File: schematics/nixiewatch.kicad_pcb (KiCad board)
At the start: 2 copper layers, 70 x 50 mm, 21 parts, among them Q1 BC546, Q2 6N90C, U1 NE555P

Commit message: pcb layout
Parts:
- removed +BATT: +8V, Connector_Pin:Pin_D0.7mm_L6.5mm_W1.8mm_FlatFork
- removed REF**: GND, Connector_Pin:Pin_D0.7mm_L6.5mm_W1.8mm_FlatFork
- removed REF**: +170V, Connector_Pin:Pin_D0.7mm_L6.5mm_W1.8mm_FlatFork
- added C5: 33u, Capacitor_THT:CP_Radial_D4.0mm_P1.50mm, F.Cu at (83.6, 129.8)
- added N1: IN-16, Connector_PinHeader_2.00mm:PinHeader_1x13_P2.00mm_Vertical, F.Cu at (48.9, 169.8)
- added N2: IN-16, Connector_PinHeader_2.00mm:PinHeader_1x13_P2.00mm_Vertical, F.Cu at (101.4, 169.8)
- added Q3: BC546, Package_TO_SOT_THT:TO-92_Inline, F.Cu at (63.0, 148.6)
- added R10: 20k, Resistor_THT:R_Axial_DIN0207_L6.3mm_D2.5mm_P7.62mm_Horizontal, F.Cu at (71.2, 123.2)
- added R11: 20k, Resistor_THT:R_Axial_DIN0207_L6.3mm_D2.5mm_P7.62mm_Horizontal, F.Cu at (64.3, 129.6)
- added R12: 47k, Resistor_THT:R_Axial_DIN0207_L6.3mm_D2.5mm_P7.62mm_Horizontal, F.Cu at (87.5, 151.6)
- added R13: 6k8, Resistor_THT:R_Axial_DIN0207_L6.3mm_D2.5mm_P7.62mm_Horizontal, F.Cu at (61.0, 146.0)
- added R14: 2k2, Resistor_THT:R_Axial_DIN0207_L6.3mm_D2.5mm_P7.62mm_Horizontal, F.Cu at (81.4, 151.6)
- added R15: 20k, Resistor_THT:R_Axial_DIN0207_L6.3mm_D2.5mm_P7.62mm_Horizontal, F.Cu at (67.5, 151.7)
- added R16: 100k, Resistor_THT:R_Axial_DIN0207_L6.3mm_D2.5mm_P7.62mm_Horizontal, F.Cu at (68.4, 166.8)
- added R17: 100k, Resistor_THT:R_Axial_DIN0207_L6.3mm_D2.5mm_P7.62mm_Horizontal, F.Cu at (86.7, 166.8)
- added R18: 100k, Resistor_THT:R_Axial_DIN0207_L6.3mm_D2.5mm_P7.62mm_Horizontal, F.Cu at (101.4, 161.2)
- added R19: 100k, Resistor_THT:R_Axial_DIN0207_L6.3mm_D2.5mm_P7.62mm_Horizontal, F.Cu at (101.4, 143.8)
- added R9: 20k, Resistor_THT:R_Axial_DIN0207_L6.3mm_D2.5mm_P7.62mm_Horizontal, F.Cu at (71.2, 119.8)
- added U2: TPIC6B595, Package_DIP:DIP-20_W7.62mm, F.Cu at (50.4, 142.8)
- added U3: 5V MCP1702, Package_TO_SOT_THT:TO-92_Inline, F.Cu at (83.6, 135.7)
- added U4: TPIC6B595, Package_DIP:DIP-20_W7.62mm, F.Cu at (63.4, 164.2)
- added U5: TPIC6B595, Package_DIP:DIP-20_W7.62mm, F.Cu at (91.0, 143.2)
- added U6: ATtiny45V-10P, Package_DIP:DIP-8_W7.62mm, F.Cu at (64.4, 132.7)
- added U7: DS1307+, Package_DIP:DIP-8_W7.62mm, F.Cu at (78.2, 144.0)
- added Y1: 32.768kHz 12.5pF, Crystal:Crystal_C38-LF_D3.0mm_L8.0mm_Horizontal, F.Cu at (78.0, 142.1)
- C2: value 330u -> 100n; footprint Capacitor_THT:CP_Radial_D8.0mm_P3.50mm -> Capacitor_THT:C_Disc_D3.0mm_W2.0mm_P2.50mm
- C3: value 100p -> 33u; footprint Capacitor_THT:C_Disc_D3.0mm_W2.0mm_P2.50mm -> Capacitor_THT:CP_Radial_D4.0mm_P1.50mm
- C4: value 4u7 400V -> 1u 200V; footprint Capacitor_THT:CP_Radial_D8.0mm_P3.50mm -> Capacitor_THT:CP_Radial_D5.0mm_P2.50mm
- D1: value 200V -> 1N4007; footprint Diode_THT:D_A-405_P12.70mm_Horizontal -> Diode_THT:D_DO-41_SOD81_P10.16mm_Horizontal
- L1: value 287u -> 180u; footprint Inductor_THT:L_Toroid_Horizontal_D21.8mm_P19.60mm_Bourns_2100 -> Inductor_THT:L_Radial_D12.0mm_P5.00mm_Neosid_SD12k_style2
- Q2: value 6N90C -> IPU80R1K0CE; footprint Package_TO_SOT_THT:TO-220F-3_Horizontal_TabDown -> Package_TO_SOT_THT:SIPAK-1EP_Horizontal_TabDown
- R7: value 640k -> 680k
- moved D1 125.3 mm to (60.6, 125.0), turned to -90 degrees
- moved C4 122.7 mm to (74.6, 127.8), turned to 0 degrees
- moved R7 121.6 mm to (63.6, 126.4), turned to 0 degrees
- moved Q2 113.4 mm to (56.7, 136.5), turned to 90 degrees
- moved R6 108.5 mm to (84.5, 151.6), turned to 90 degrees
- moved R5 103.6 mm to (56.9, 139.4), turned to 180 degrees
- moved L1 100.8 mm to (50.1, 124.3)
- moved RV1 98.7 mm to (78.5, 123.9), turned to 90 degrees
- moved R8 90.2 mm to (81.8, 118.0)
- moved Q1 90.0 mm to (87.7, 124.0), turned to 180 degrees
- moved C3 89.9 mm to (82.5, 139.8), turned to 0 degrees
- moved R1 77.0 mm to (98.6, 123.4), turned to 180 degrees
- moved R4 75.9 mm to (98.6, 140.0), turned to 180 degrees
- moved U1 70.0 mm to (98.6, 126.0)
- moved C1 69.8 mm to (101.4, 123.7), turned to -90 degrees
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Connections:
- C3 pad 1: Net-(C3-Pad1) -> +BATT
- R6 pad 1: Net-(D1-A) -> Net-(U2-VCC)
- R6 pad 2: Net-(C3-Pad1) -> Net-(U6-PB2)
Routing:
- net Net-(U2-VCC): track 0.00 -> 135.5 mm
- net GND: track 108.5 -> 216.1 mm, vias 0 -> 1
- net Net-(N2-PadA): track 0.00 -> 80.8 mm
- net Net-(U2-SRCK): track 0.00 -> 78.3 mm, vias 0 -> 1
- net Net-(Q3-C): track 0.00 -> 76.9 mm, vias 0 -> 1
- net Net-(N1-PadA): track 0.00 -> 71.3 mm
- net Net-(U1-OUT): track 2.54 -> 71.8 mm
- net Net-(Q1-C): track 54.7 -> 13.8 mm
- net Net-(U6-PB2): track 0.00 -> 30.6 mm
- net Net-(Q2-G): track 33.1 -> 2.99 mm
- net Net-(U4-DRAIN7): track 0.00 -> 29.7 mm
- net Net-(N2-PadRHDP): track 0.00 -> 29.3 mm
- net Net-(U2-SER_OUT): track 0.00 -> 27.2 mm
- net Net-(U4-SER_OUT): track 0.00 -> 26.9 mm
- net Net-(U2-DRAIN7): track 0.00 -> 25.4 mm
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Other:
- board outline removed

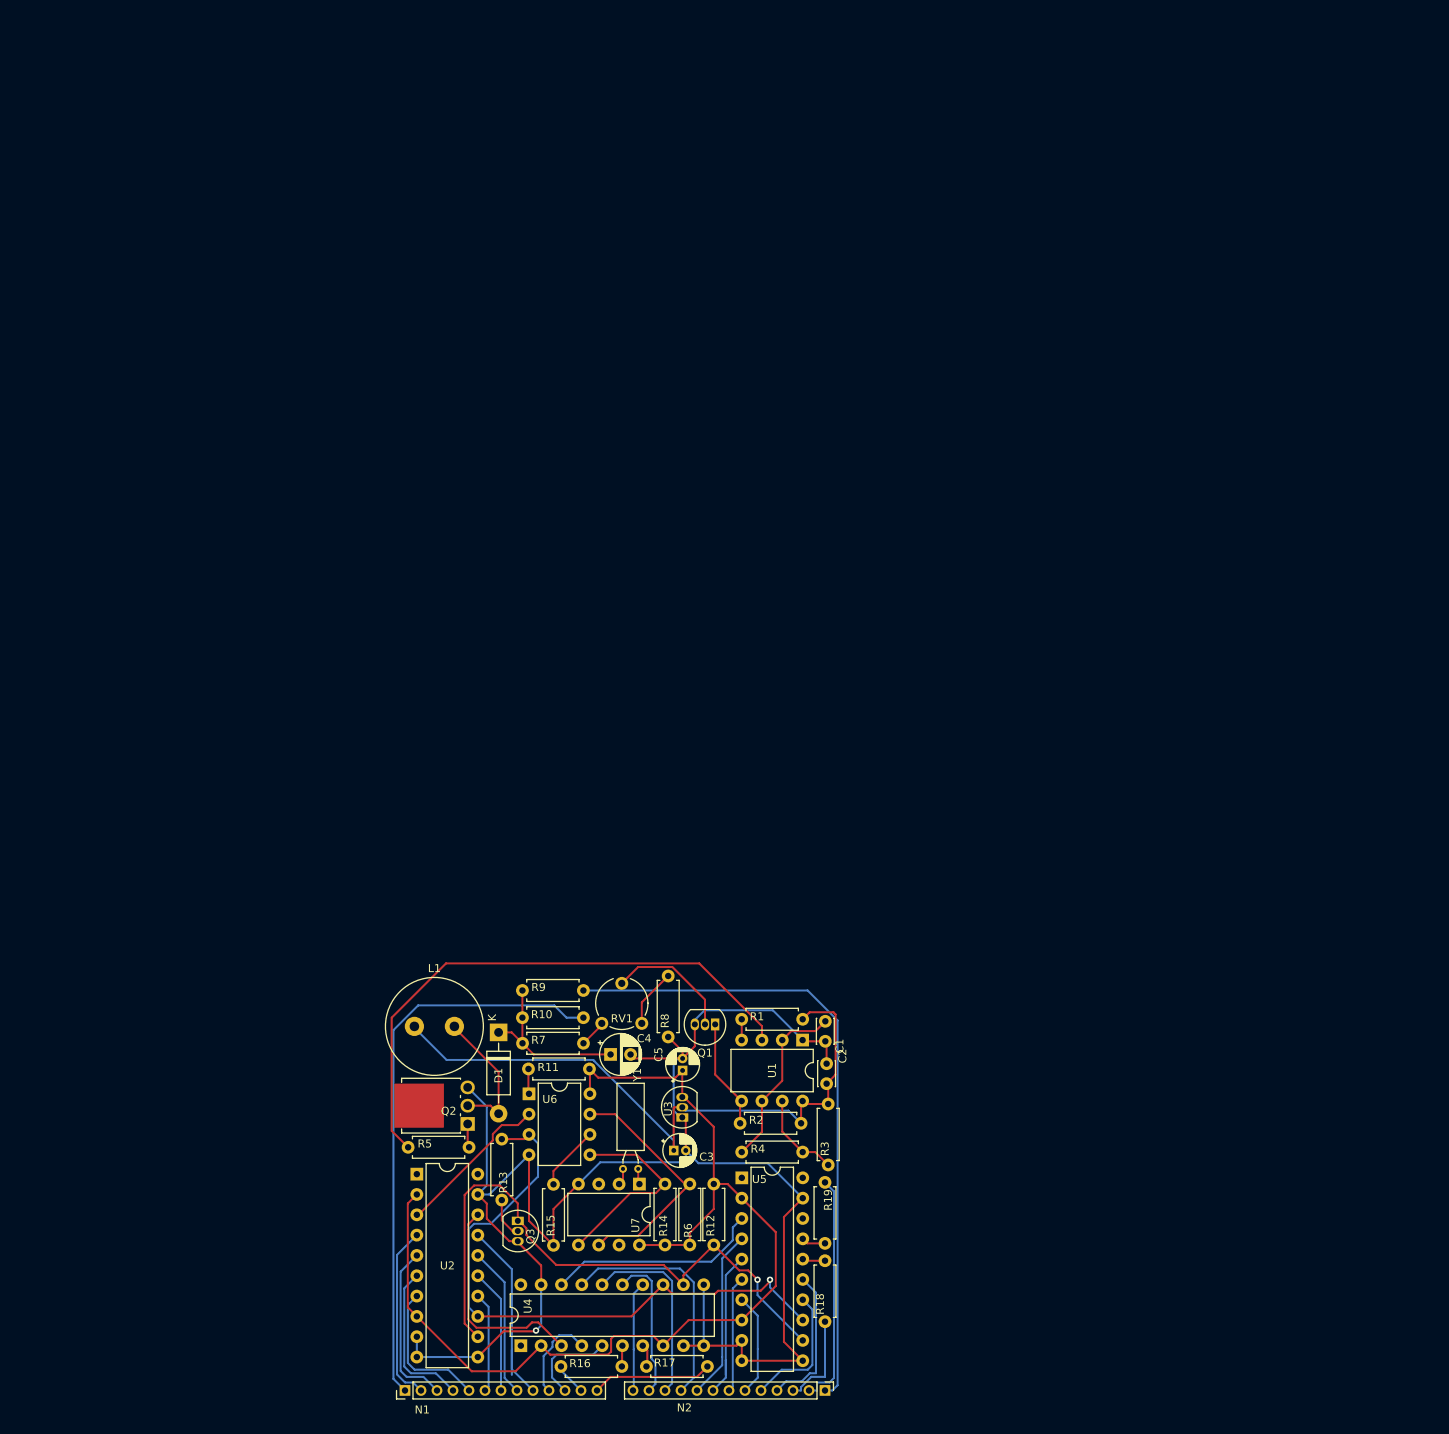
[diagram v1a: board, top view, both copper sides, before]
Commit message: cleaned up the schematic
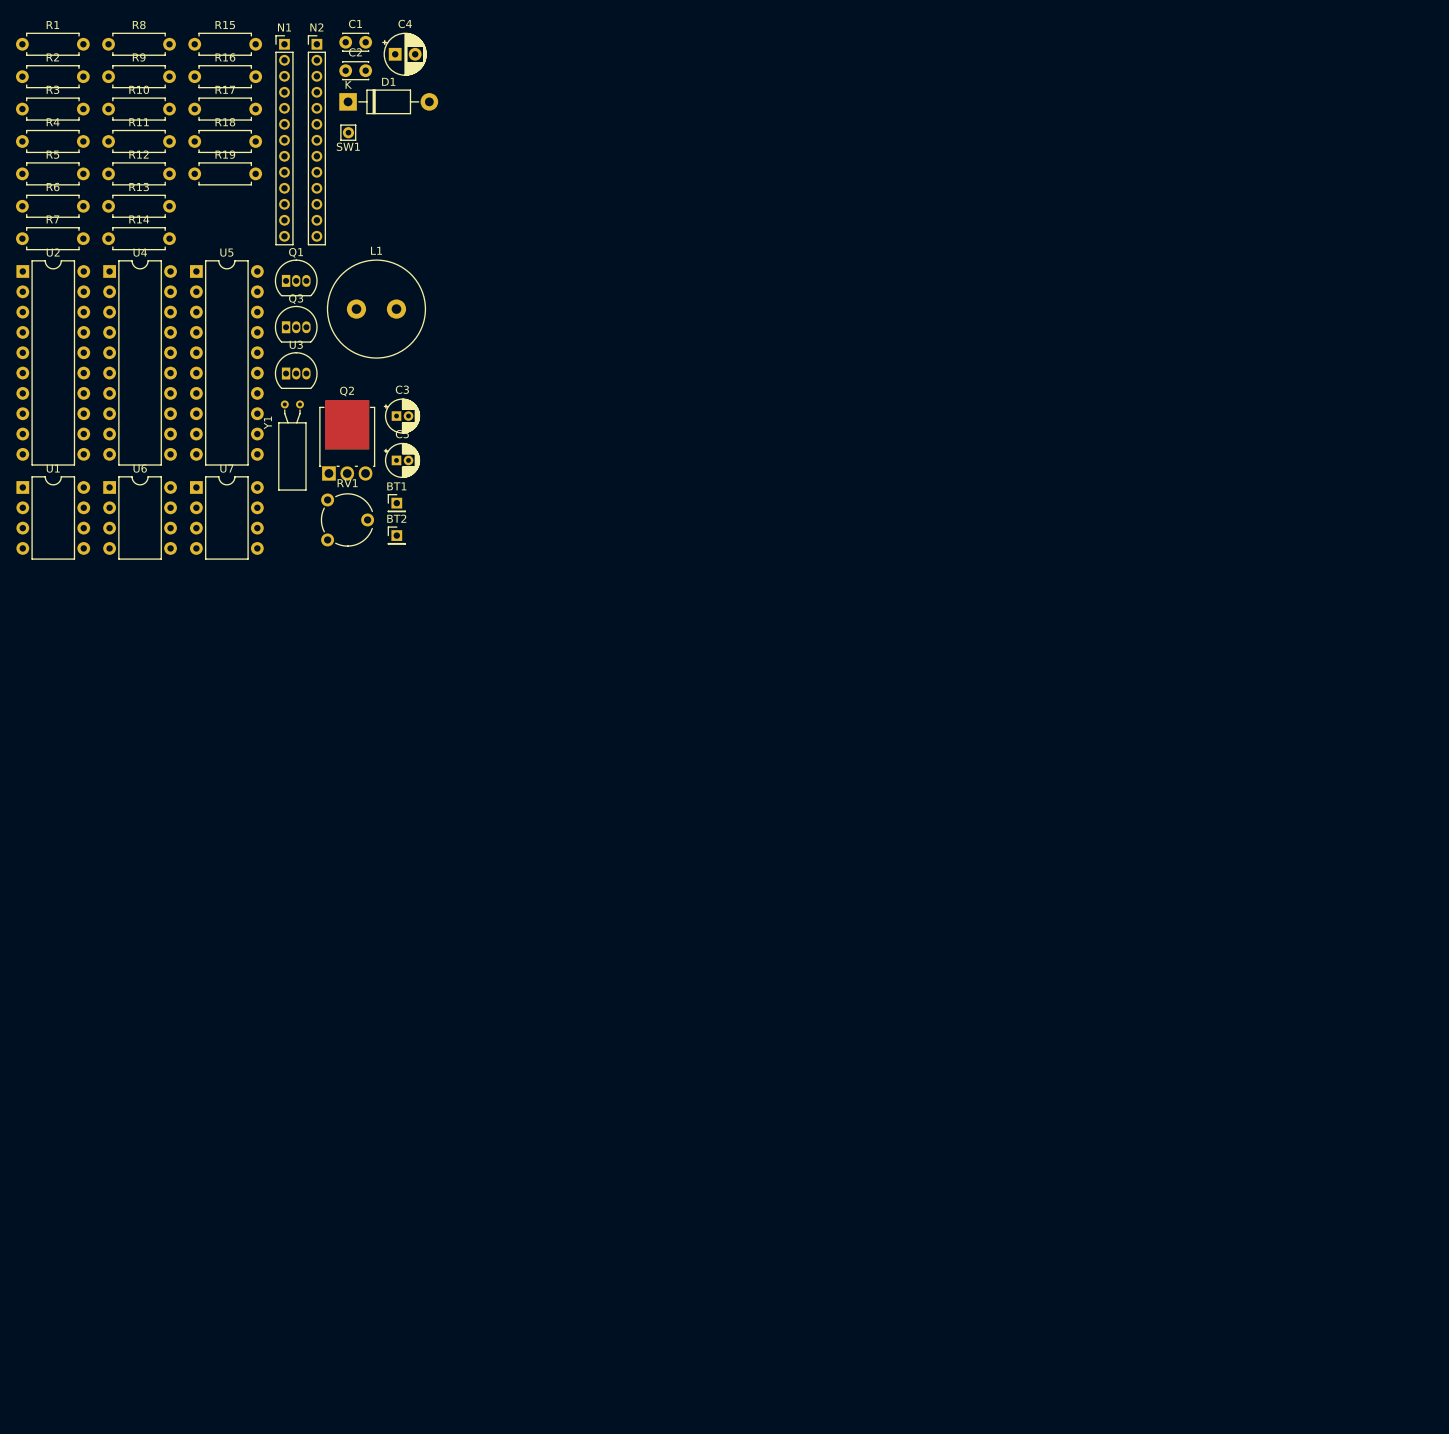
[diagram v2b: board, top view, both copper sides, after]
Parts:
- added BT1: 8.4V, Connector_PinHeader_2.00mm:PinHeader_1x01_P2.00mm_Vertical, F.Cu at (47.9, 58.9)
- added BT2: 3V, Connector_PinHeader_2.00mm:PinHeader_1x01_P2.00mm_Vertical, F.Cu at (47.9, 62.9)
- added SW1: SW_Push, Connector_Pin:Pin_D0.7mm_L6.5mm_W1.8mm_FlatFork, F.Cu at (41.8, 12.6)
- R11: value 20k -> 10k
- U3: value 5V MCP1702 -> MCP1702-5002E/TO
- moved N2 179.9 mm to (37.9, 1.52), turned to 0 degrees
- moved R17 169.7 mm to (22.6, 9.62), turned to 0 degrees
- moved N1 168.9 mm to (33.8, 1.52), turned to 0 degrees
- moved R16 167.6 mm to (22.6, 5.58)
- moved R18 167.2 mm to (22.6, 13.7), turned to 0 degrees
- moved R2 163.1 mm to (1.07, 5.58), turned to 0 degrees
- moved R3 160.0 mm to (1.07, 9.62), turned to 0 degrees
- moved R4 159.6 mm to (1.07, 13.7), turned to 0 degrees
- moved R15 156.7 mm to (22.6, 1.52), turned to 0 degrees
- moved R1 156.1 mm to (1.07, 1.52), turned to 0 degrees
- moved R6 154.3 mm to (1.07, 21.8), turned to 0 degrees
- moved R12 153.8 mm to (11.8, 17.7), turned to 0 degrees
- moved R19 148.7 mm to (22.6, 17.7), turned to 0 degrees
- moved U4 143.8 mm to (12.0, 29.9), turned to 0 degrees
- moved R14 143.7 mm to (11.8, 25.8), turned to 0 degrees
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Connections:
- N1 pad 1: Net-(N1-PadA) -> Net-(U2-DRAIN1)
- N1 pad 10: Net-(U4-DRAIN0) -> (no net)
- N1 pad 11: Net-(U4-DRAIN1) -> (no net)
- N1 pad 12: Net-(N1-PadLHDP) -> (no net)
- N1 pad 13: Net-(N1-PadRHDP) -> (no net)
- N1 pad 2: Net-(U2-DRAIN0) -> Net-(U2-DRAIN2)
- N1 pad 3: Net-(U2-DRAIN1) -> Net-(U2-DRAIN3)
- N1 pad 4: Net-(U2-DRAIN2) -> Net-(U2-DRAIN4)
- N1 pad 5: Net-(U2-DRAIN3) -> Net-(U2-DRAIN5)
- N1 pad 6: Net-(U2-DRAIN4) -> Net-(U2-DRAIN6)
- N1 pad 7: Net-(U2-DRAIN5) -> Net-(U2-DRAIN7)
- N1 pad 8: Net-(U2-DRAIN6) -> Net-(U4-DRAIN0)
- N1 pad 9: Net-(U2-DRAIN7) -> Net-(U4-DRAIN1)
- N2 pad 1: Net-(N2-PadA) -> Net-(U4-DRAIN5)
- N2 pad 10: Net-(U4-DRAIN7) -> (no net)
- N2 pad 11: Net-(U4-DRAIN6) -> (no net)
- N2 pad 12: Net-(U4-DRAIN5) -> (no net)
- N2 pad 13: Net-(U4-DRAIN4) -> (no net)
- N2 pad 2: Net-(N2-PadRHDP) -> Net-(U4-DRAIN6)
- N2 pad 3: Net-(N2-PadLHDP) -> Net-(U4-DRAIN7)
- N2 pad 4: Net-(U5-DRAIN5) -> Net-(U5-DRAIN0)
- N2 pad 5: Net-(U5-DRAIN4) -> Net-(U5-DRAIN1)
- N2 pad 6: Net-(U5-DRAIN3) -> Net-(U5-DRAIN2)
- N2 pad 7: Net-(U5-DRAIN2) -> Net-(U5-DRAIN3)
- N2 pad 8: Net-(U5-DRAIN1) -> Net-(U5-DRAIN4)
- N2 pad 9: Net-(U5-DRAIN0) -> Net-(U5-DRAIN5)
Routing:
- net GND: track 216.1 -> 0.00 mm, vias 1 -> 0
- net Net-(U2-VCC): track 135.5 -> 0.00 mm
- net +BATT: track 84.4 -> 0.00 mm
- net Net-(N2-PadA): track 80.8 -> 0.00 mm
- net Net-(U2-SRCK): track 78.3 -> 0.00 mm, vias 1 -> 0
- net Net-(Q3-C): track 76.9 -> 0.00 mm, vias 1 -> 0
- net Net-(U1-OUT): track 71.8 -> 0.00 mm
- net Net-(N1-PadA): track 71.3 -> 0.00 mm
- net Net-(U6-PB2): track 30.6 -> 0.00 mm
- net Net-(U4-DRAIN7): track 29.7 -> 0.00 mm
- net Net-(N2-PadRHDP): track 29.3 -> 0.00 mm
- net Net-(U2-SER_OUT): track 27.2 -> 0.00 mm
- net Net-(U4-SER_OUT): track 26.9 -> 0.00 mm
- net Net-(U2-DRAIN7): track 25.4 -> 0.00 mm
- net Net-(U6-AREF/PB0): track 24.9 -> 0.00 mm
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
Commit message: pcb
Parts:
- removed BT2: 3V, Connector_PinHeader_2.00mm:PinHeader_1x01_P2.00mm_Vertical
- removed N1, N2: IN-16, Connector_PinHeader_2.00mm:PinHeader_1x13_P2.00mm_Vertical
- removed R10, R9: 20k, Resistor_THT:R_Axial_DIN0207_L6.3mm_D2.5mm_P7.62mm_Horizontal
- removed R16, R17, R18, R19: 100k, Resistor_THT:R_Axial_DIN0207_L6.3mm_D2.5mm_P7.62mm_Horizontal
- removed SW1: SW_Push, Connector_Pin:Pin_D0.7mm_L6.5mm_W1.8mm_FlatFork
- added G***: LOGO, LOGO, F.Cu at (53.4, 25.4)
- added G***: LOGO, LOGO, F.Cu at (31.5, 69.8)
- added H1: MountingHole, MountingHole:MountingHole_2.2mm_M2, F.Cu at (65.6, 27.0)
- added H2: MountingHole, MountingHole:MountingHole_2.2mm_M2, F.Cu at (82.0, 27.0)
- added J1: Conn_01x25, Connector_PinHeader_2.00mm:PinHeader_1x24_P2.00mm_Vertical, F.Cu at (36.1, 70.5)
- added J10: BT2_3V, Connector_PinHeader_2.00mm:PinHeader_1x01_P2.00mm_Vertical, F.Cu at (58.0, 46.8)
- added J2: ButtonL, Connector_PinHeader_2.00mm:PinHeader_1x01_P2.00mm_Vertical, F.Cu at (49.2, 50.0)
- added J4: ButtonH, Connector_PinHeader_2.00mm:PinHeader_1x01_P2.00mm_Vertical, F.Cu at (67.5, 36.6)
- added J7: ButtonH, Connector_PinHeader_2.00mm:PinHeader_1x01_P2.00mm_Vertical, F.Cu at (57.1, 32.7)
- added J9: BT2GND, Connector_PinHeader_2.00mm:PinHeader_1x01_P2.00mm_Vertical, F.Cu at (31.6, 54.0)
- added REF**: Symbol_Highvoltage_Type1_CopperTop_Small, Symbol:Symbol_Highvoltage_Type1_CopperTop_Small, B.Cu at (36.4, 32.4)
- BT1: footprint Connector_PinHeader_2.00mm:PinHeader_1x01_P2.00mm_Vertical -> Connector_PinHeader_2.00mm:PinHeader_1x02_P2.00mm_Vertical
- moved R3 88.6 mm to (83.8, 41.4), turned to 180 degrees
- moved U1 81.8 mm to (78.2, 29.8), turned to -90 degrees
- moved R1 81.2 mm to (78.1, 27.0), turned to 180 degrees
- moved R2 81.0 mm to (70.5, 47.3), turned to 90 degrees
- moved R4 79.9 mm to (73.5, 47.3), turned to 90 degrees
- moved R6 77.1 mm to (69.6, 57.1), turned to 90 degrees
- moved R12 72.6 mm to (72.8, 57.1), turned to 90 degrees
- moved U4 66.7 mm to (71.6, 59.9), turned to -90 degrees
- moved R15 63.1 mm to (52.6, 57.0), turned to 90 degrees
- moved R14 62.9 mm to (66.5, 57.1), turned to 90 degrees
- moved R8 57.9 mm to (58.0, 36.5), turned to -90 degrees
- moved U5 55.3 mm to (76.2, 44.5)
- moved C2 52.2 mm to (81.1, 38.8), turned to 90 degrees
- moved C1 49.9 mm to (81.1, 31.6), turned to -90 degrees
- moved R13 46.8 mm to (44.8, 55.0), turned to 90 degrees
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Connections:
- net Net-(D1-A) renamed /170V_int
- net Net-(Q3-C) renamed /RCK
- net Net-(U2-SER_IN) renamed /SERIAL_DATA
- net Net-(U2-SRCK) renamed /SRCK
- net Net-(U2-VCC) renamed +5V
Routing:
- net +5V: track 0.00 -> 131.9 mm
- net +BATT: track 0.00 -> 111.5 mm
- net /SRCK: track 0.00 -> 76.1 mm, vias 0 -> 3
- net /RCK: track 0.00 -> 66.0 mm, vias 0 -> 1
- net Net-(U1-Q): track 0.00 -> 60.2 mm
- net Net-(U6-PB2): track 0.00 -> 38.6 mm
- net Net-(U2-SER_OUT): track 0.00 -> 37.2 mm
- net +170V: track 0.00 -> 26.5 mm
- net Net-(U6-AREF/PB0): track 0.00 -> 26.3 mm
- net Net-(J1-Pin_23): track 0.00 -> 26.3 mm
- net Net-(J1-Pin_1): track 0.00 -> 24.1 mm, vias 0 -> 1
- net Net-(U4-SER_OUT): track 0.00 -> 22.0 mm
- net Net-(J1-Pin_8): track 0.00 -> 21.9 mm
- net Net-(J1-Pin_9): track 0.00 -> 21.8 mm
- net Net-(J1-Pin_17): track 0.00 -> 21.7 mm
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- added copper zone on B.Cu, net GND
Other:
- board outline added: 56.8 x 49.8 mm
- board text added: "Nixie Watch v1.0"
